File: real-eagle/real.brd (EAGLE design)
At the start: 104.1 x 123.4 mm, 49 parts, among them J2 POWER_JACK

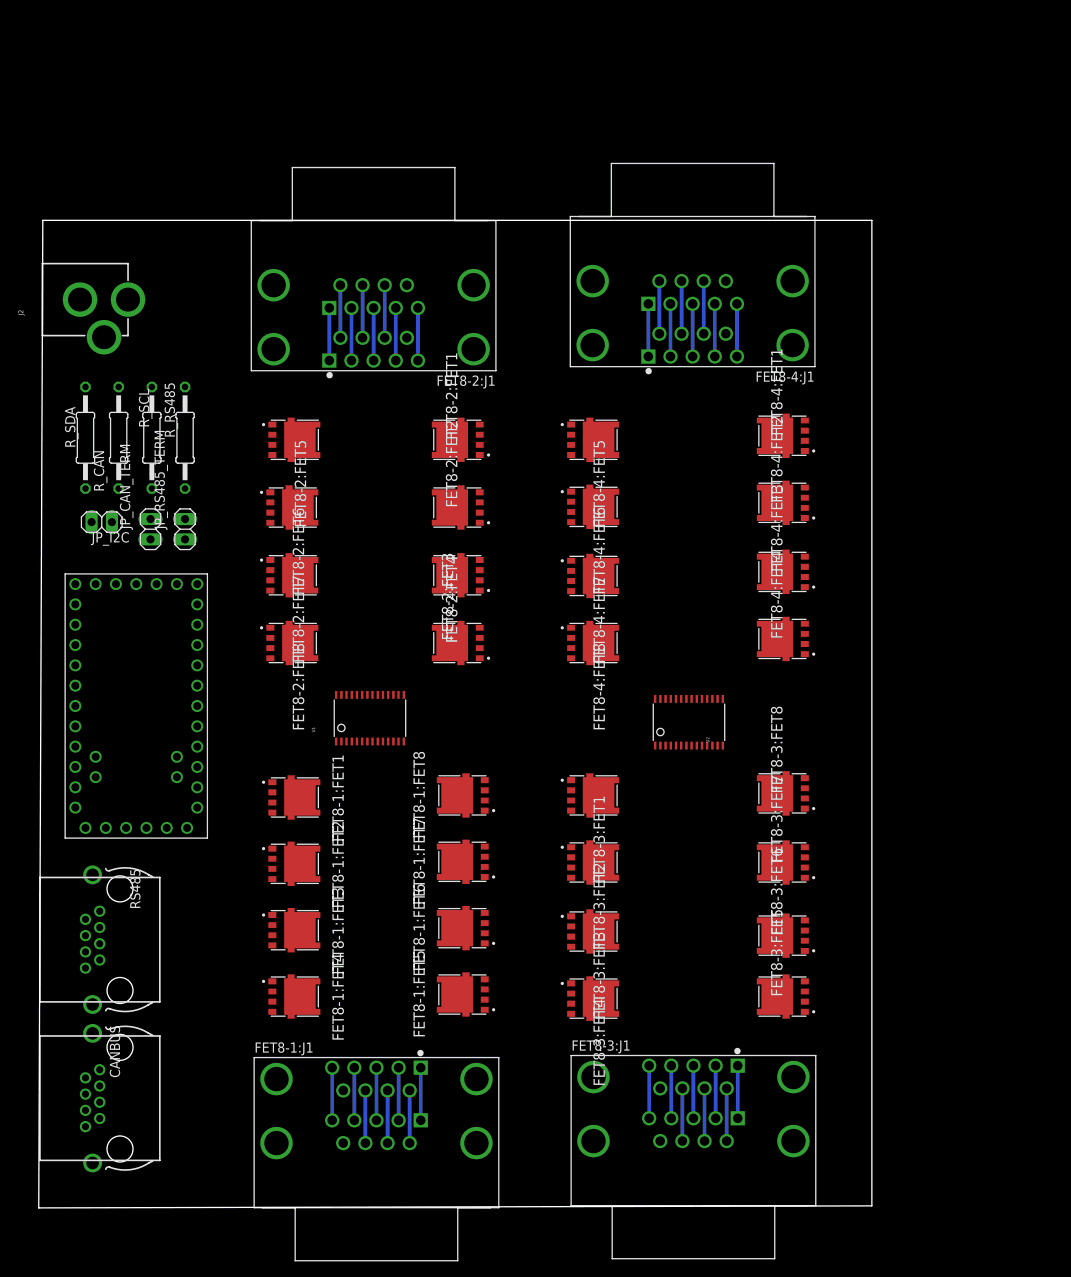
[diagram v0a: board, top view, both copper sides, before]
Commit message: Basis for routing
Route commands:

auto PWM_A0 PWM_A1 PWM_A2 PWM_A3 PWM_A4 PWM_A5 PWM_A6 PWM_A7 HEATER_A0 HEATER_A1 HEATER_A2 HEATER_A3 HEATER_A4 HEATER_A5 HEATER_A6 HEATER_A7 PWM_B0 PWM_B1 PWM_B2 PWM_B3 PWM_B4 PWM_B5 PWM_B6 PWM_B7 HEATER_B0 HEATER_B1 HEATER_B2 HEATER_B3 HEATER_B4 HEATER_B5 HEATER_B6 HEATER_B7

auto PWM_C0 PWM_C1 PWM_C2 PWM_C3 PWM_C4 PWM_C5 PWM_C6 PWM_C7 HEATER_C0 HEATER_C1 HEATER_C2 HEATER_C3 HEATER_C4 HEATER_C5 HEATER_C6 HEATER_C7 PWM_D0 PWM_D1 PWM_D2 PWM_D3 PWM_D4 PWM_D5 PWM_D6 PWM_D7 HEATER_D0 HEATER_D1 HEATER_D2 HEATER_D3 HEATER_D4 HEATER_D5 HEATER_D6 HEATER_D7

auto ! gnd
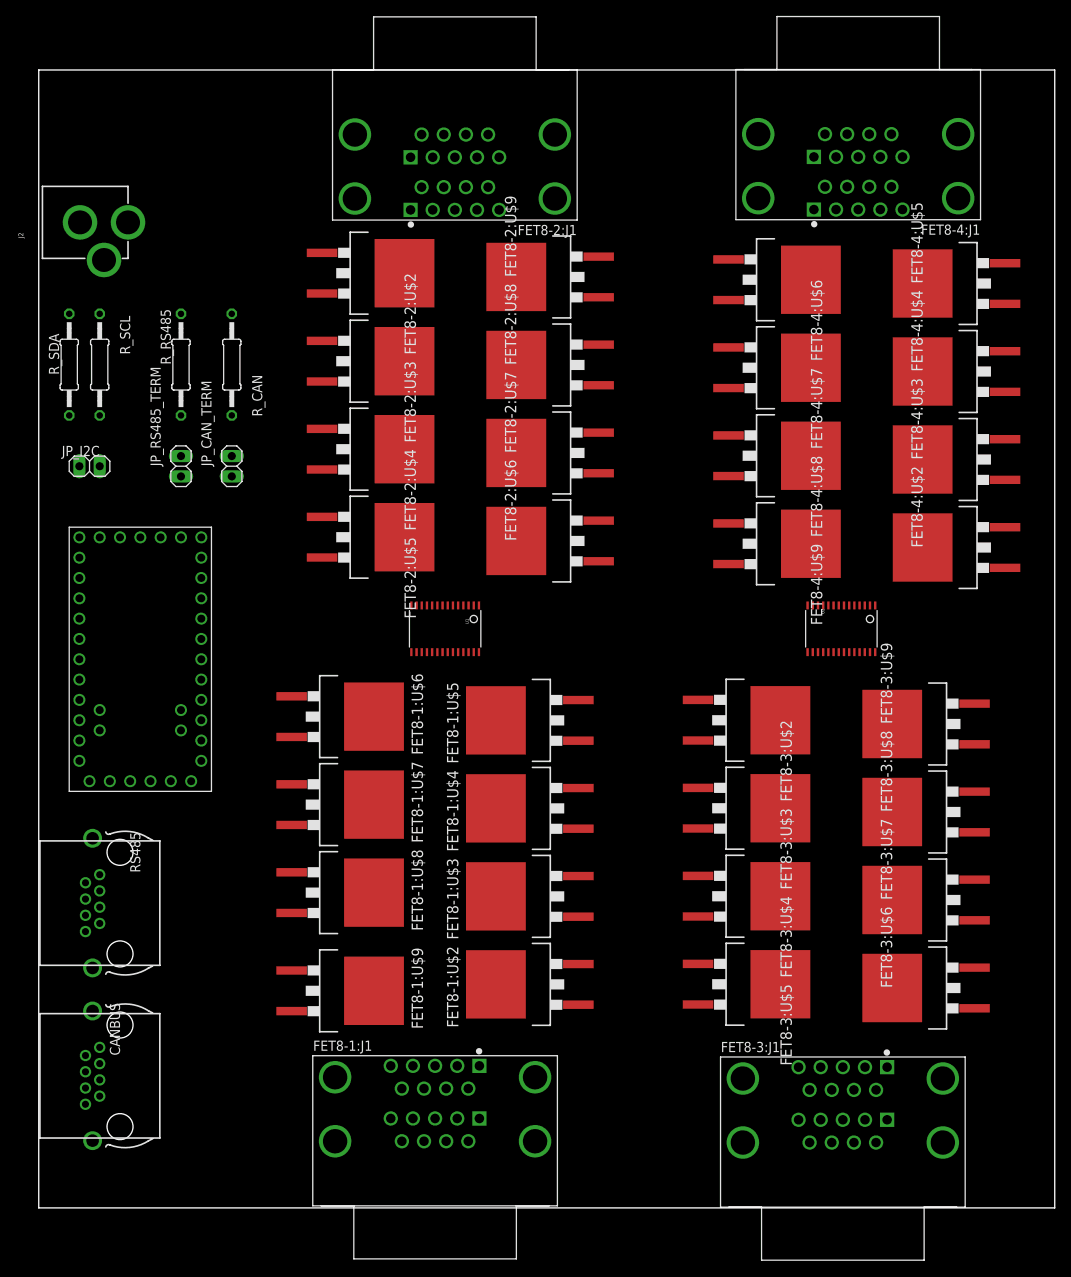
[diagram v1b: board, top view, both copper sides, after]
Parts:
- removed FET8-1:FET1, FET8-1:FET2, FET8-1:FET3, FET8-1:FET4, FET8-1:FET5, FET8-1:FET6, FET8-1:FET7, FET8-1:FET8, FET8-2:FET1, FET8-2:FET2, FET8-2:FET3, FET8-2:FET4, FET8-2:FET5, FET8-2:FET6, FET8-2:FET7, FET8-2:FET8, FET8-3:FET1, FET8-3:FET2, FET8-3:FET3, FET8-3:FET4, FET8-3:FET5, FET8-3:FET6, FET8-3:FET7, FET8-3:FET8, FET8-4:FET1, FET8-4:FET2, FET8-4:FET3, FET8-4:FET4, FET8-4:FET5, FET8-4:FET6, FET8-4:FET7, FET8-4:FET8: ONSEMI_FET_NVMFS5C604NL, real_library:DFN500X600X110-5N
- added FET8-1:U$2, FET8-1:U$3, FET8-1:U$4, FET8-1:U$5, FET8-1:U$6, FET8-1:U$7, FET8-1:U$8, FET8-1:U$9, FET8-2:U$2, FET8-2:U$3, FET8-2:U$4, FET8-2:U$5, FET8-2:U$6, FET8-2:U$7, FET8-2:U$8, FET8-2:U$9, FET8-3:U$2, FET8-3:U$3, FET8-3:U$4, FET8-3:U$5, FET8-3:U$6, FET8-3:U$7, FET8-3:U$8, FET8-3:U$9, FET8-4:U$2, FET8-4:U$3, FET8-4:U$4, FET8-4:U$5, FET8-4:U$6, FET8-4:U$7, FET8-4:U$8, FET8-4:U$9: NEXFET_CSD18542KTT, real_library:D2PAK-KTT
- moved FET8-4:J1 27.7 mm to (96.9, 91.8)
- moved U2 22.3 mm to (100.3, 39.4), turned to 180 degrees
- moved FET8-2:J1 21.4 mm to (46.5, 91.7)
- moved FET8-3:J1 18.7 mm to (106.1, -15.4)
- moved U1 14.6 mm to (50.8, 39.4), turned to 180 degrees
- moved R_CAN 13.5 mm to (24.1, 72.4)
- moved JP_CAN_TERM 12.9 mm to (24.1, 59.7)
- moved J2 9.65 mm to (-2.54, 90.2)
- moved R_SCL 9.45 mm to (7.62, 72.4)
- moved R_SDA 9.37 mm to (3.81, 72.4)
- moved R_RS485 9.16 mm to (17.8, 72.4)
- moved JP_RS485_TERM 7.89 mm to (17.8, 59.7)
- moved FET8-1:J1 7.33 mm to (55.1, -15.3)
- moved JP_I2C 7.15 mm to (6.35, 59.7), turned to 180 degrees
- moved U$1 5.86 mm to (12.7, 35.6)
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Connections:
- net GND: now also FET8-1:U$2.3, FET8-1:U$3.3, FET8-1:U$4.3, FET8-1:U$5.3, FET8-1:U$6.3, FET8-1:U$7.3, FET8-1:U$8.3, FET8-1:U$9.3, FET8-2:U$2.3, FET8-2:U$3.3, FET8-2:U$4.3, FET8-2:U$5.3, FET8-2:U$6.3, FET8-2:U$7.3, FET8-2:U$8.3, FET8-2:U$9.3, FET8-3:U$2.3, FET8-3:U$3.3, FET8-3:U$4.3, FET8-3:U$5.3, FET8-3:U$6.3, FET8-3:U$7.3, FET8-3:U$8.3, FET8-3:U$9.3, FET8-4:U$2.3, FET8-4:U$3.3, FET8-4:U$4.3, FET8-4:U$5.3, FET8-4:U$6.3, FET8-4:U$7.3, FET8-4:U$8.3, FET8-4:U$9.3; no longer FET8-1:FET1.1, FET8-1:FET1.2, FET8-1:FET1.3, FET8-1:FET2.1, FET8-1:FET2.2, FET8-1:FET2.3, FET8-1:FET3.1, FET8-1:FET3.2, FET8-1:FET3.3, FET8-1:FET4.1, FET8-1:FET4.2, FET8-1:FET4.3, FET8-1:FET5.1, FET8-1:FET5.2, FET8-1:FET5.3, FET8-1:FET6.1, FET8-1:FET6.2, FET8-1:FET6.3, FET8-1:FET7.1, FET8-1:FET7.2, FET8-1:FET7.3, FET8-1:FET8.1, FET8-1:FET8.2, FET8-1:FET8.3, FET8-2:FET1.1, FET8-2:FET1.2, FET8-2:FET1.3, FET8-2:FET2.1, FET8-2:FET2.2, FET8-2:FET2.3, FET8-2:FET3.1, FET8-2:FET3.2, FET8-2:FET3.3, FET8-2:FET4.1, FET8-2:FET4.2, FET8-2:FET4.3, FET8-2:FET5.1, FET8-2:FET5.2, FET8-2:FET5.3, FET8-2:FET6.1, FET8-2:FET6.2, FET8-2:FET6.3, FET8-2:FET7.1, FET8-2:FET7.2, FET8-2:FET7.3, FET8-2:FET8.1, FET8-2:FET8.2, FET8-2:FET8.3, FET8-3:FET1.1, FET8-3:FET1.2, FET8-3:FET1.3, FET8-3:FET2.1, FET8-3:FET2.2, FET8-3:FET2.3, FET8-3:FET3.1, FET8-3:FET3.2, FET8-3:FET3.3, FET8-3:FET4.1, FET8-3:FET4.2, FET8-3:FET4.3, FET8-3:FET5.1, FET8-3:FET5.2, FET8-3:FET5.3, FET8-3:FET6.1, FET8-3:FET6.2, FET8-3:FET6.3, FET8-3:FET7.1, FET8-3:FET7.2, FET8-3:FET7.3, FET8-3:FET8.1, FET8-3:FET8.2, FET8-3:FET8.3, FET8-4:FET1.1, FET8-4:FET1.2, FET8-4:FET1.3, FET8-4:FET2.1, FET8-4:FET2.2, FET8-4:FET2.3, FET8-4:FET3.1, FET8-4:FET3.2, FET8-4:FET3.3, FET8-4:FET4.1, FET8-4:FET4.2, FET8-4:FET4.3, FET8-4:FET5.1, FET8-4:FET5.2, FET8-4:FET5.3, FET8-4:FET6.1, FET8-4:FET6.2, FET8-4:FET6.3, FET8-4:FET7.1, FET8-4:FET7.2, FET8-4:FET7.3, FET8-4:FET8.1, FET8-4:FET8.2, FET8-4:FET8.3
- net HEATER_A0: now also FET8-1:U$2.2; no longer FET8-1:FET1.5@1, FET8-1:FET1.5@2, FET8-1:FET1.5@3, FET8-1:FET1.5@4, FET8-1:FET1.5@5
- net HEATER_A1: now also FET8-1:U$3.2; no longer FET8-1:FET2.5@1, FET8-1:FET2.5@2, FET8-1:FET2.5@3, FET8-1:FET2.5@4, FET8-1:FET2.5@5
- net HEATER_A2: now also FET8-1:U$4.2; no longer FET8-1:FET3.5@1, FET8-1:FET3.5@2, FET8-1:FET3.5@3, FET8-1:FET3.5@4, FET8-1:FET3.5@5
- net HEATER_A3: now also FET8-1:U$5.2; no longer FET8-1:FET4.5@1, FET8-1:FET4.5@2, FET8-1:FET4.5@3, FET8-1:FET4.5@4, FET8-1:FET4.5@5
- net HEATER_A4: now also FET8-1:U$6.2; no longer FET8-1:FET5.5@1, FET8-1:FET5.5@2, FET8-1:FET5.5@3, FET8-1:FET5.5@4, FET8-1:FET5.5@5
- net HEATER_A5: now also FET8-1:U$7.2; no longer FET8-1:FET6.5@1, FET8-1:FET6.5@2, FET8-1:FET6.5@3, FET8-1:FET6.5@4, FET8-1:FET6.5@5
- net HEATER_A6: now also FET8-1:U$8.2; no longer FET8-1:FET7.5@1, FET8-1:FET7.5@2, FET8-1:FET7.5@3, FET8-1:FET7.5@4, FET8-1:FET7.5@5
- net HEATER_A7: now also FET8-1:U$9.2; no longer FET8-1:FET8.5@1, FET8-1:FET8.5@2, FET8-1:FET8.5@3, FET8-1:FET8.5@4, FET8-1:FET8.5@5
- net HEATER_B0: now also FET8-2:U$2.2; no longer FET8-2:FET1.5@1, FET8-2:FET1.5@2, FET8-2:FET1.5@3, FET8-2:FET1.5@4, FET8-2:FET1.5@5
- net HEATER_B1: now also FET8-2:U$3.2; no longer FET8-2:FET2.5@1, FET8-2:FET2.5@2, FET8-2:FET2.5@3, FET8-2:FET2.5@4, FET8-2:FET2.5@5
- net HEATER_B2: now also FET8-2:U$4.2; no longer FET8-2:FET3.5@1, FET8-2:FET3.5@2, FET8-2:FET3.5@3, FET8-2:FET3.5@4, FET8-2:FET3.5@5
- net HEATER_B3: now also FET8-2:U$5.2; no longer FET8-2:FET4.5@1, FET8-2:FET4.5@2, FET8-2:FET4.5@3, FET8-2:FET4.5@4, FET8-2:FET4.5@5
- net HEATER_B4: now also FET8-2:U$6.2; no longer FET8-2:FET5.5@1, FET8-2:FET5.5@2, FET8-2:FET5.5@3, FET8-2:FET5.5@4, FET8-2:FET5.5@5
- net HEATER_B5: now also FET8-2:U$7.2; no longer FET8-2:FET6.5@1, FET8-2:FET6.5@2, FET8-2:FET6.5@3, FET8-2:FET6.5@4, FET8-2:FET6.5@5
- net HEATER_B6: now also FET8-2:U$8.2; no longer FET8-2:FET7.5@1, FET8-2:FET7.5@2, FET8-2:FET7.5@3, FET8-2:FET7.5@4, FET8-2:FET7.5@5
- net HEATER_B7: now also FET8-2:U$9.2; no longer FET8-2:FET8.5@1, FET8-2:FET8.5@2, FET8-2:FET8.5@3, FET8-2:FET8.5@4, FET8-2:FET8.5@5
- net HEATER_C0: now also FET8-3:U$2.2; no longer FET8-3:FET1.5@1, FET8-3:FET1.5@2, FET8-3:FET1.5@3, FET8-3:FET1.5@4, FET8-3:FET1.5@5
- net HEATER_C1: now also FET8-3:U$3.2; no longer FET8-3:FET2.5@1, FET8-3:FET2.5@2, FET8-3:FET2.5@3, FET8-3:FET2.5@4, FET8-3:FET2.5@5
- net HEATER_C2: now also FET8-3:U$4.2; no longer FET8-3:FET3.5@1, FET8-3:FET3.5@2, FET8-3:FET3.5@3, FET8-3:FET3.5@4, FET8-3:FET3.5@5
- net HEATER_C3: now also FET8-3:U$5.2; no longer FET8-3:FET4.5@1, FET8-3:FET4.5@2, FET8-3:FET4.5@3, FET8-3:FET4.5@4, FET8-3:FET4.5@5
- net HEATER_C4: now also FET8-3:U$6.2; no longer FET8-3:FET5.5@1, FET8-3:FET5.5@2, FET8-3:FET5.5@3, FET8-3:FET5.5@4, FET8-3:FET5.5@5
- net HEATER_C5: now also FET8-3:U$7.2; no longer FET8-3:FET6.5@1, FET8-3:FET6.5@2, FET8-3:FET6.5@3, FET8-3:FET6.5@4, FET8-3:FET6.5@5
- net HEATER_C6: now also FET8-3:U$8.2; no longer FET8-3:FET7.5@1, FET8-3:FET7.5@2, FET8-3:FET7.5@3, FET8-3:FET7.5@4, FET8-3:FET7.5@5
- net HEATER_C7: now also FET8-3:U$9.2; no longer FET8-3:FET8.5@1, FET8-3:FET8.5@2, FET8-3:FET8.5@3, FET8-3:FET8.5@4, FET8-3:FET8.5@5
- net HEATER_D0: now also FET8-4:U$2.2; no longer FET8-4:FET1.5@1, FET8-4:FET1.5@2, FET8-4:FET1.5@3, FET8-4:FET1.5@4, FET8-4:FET1.5@5
- net HEATER_D1: now also FET8-4:U$3.2; no longer FET8-4:FET2.5@1, FET8-4:FET2.5@2, FET8-4:FET2.5@3, FET8-4:FET2.5@4, FET8-4:FET2.5@5
- net HEATER_D2: now also FET8-4:U$4.2; no longer FET8-4:FET3.5@1, FET8-4:FET3.5@2, FET8-4:FET3.5@3, FET8-4:FET3.5@4, FET8-4:FET3.5@5
- net HEATER_D3: now also FET8-4:U$5.2; no longer FET8-4:FET4.5@1, FET8-4:FET4.5@2, FET8-4:FET4.5@3, FET8-4:FET4.5@4, FET8-4:FET4.5@5
- net HEATER_D4: now also FET8-4:U$6.2; no longer FET8-4:FET5.5@1, FET8-4:FET5.5@2, FET8-4:FET5.5@3, FET8-4:FET5.5@4, FET8-4:FET5.5@5
- net HEATER_D5: now also FET8-4:U$7.2; no longer FET8-4:FET6.5@1, FET8-4:FET6.5@2, FET8-4:FET6.5@3, FET8-4:FET6.5@4, FET8-4:FET6.5@5
- net HEATER_D6: now also FET8-4:U$8.2; no longer FET8-4:FET7.5@1, FET8-4:FET7.5@2, FET8-4:FET7.5@3, FET8-4:FET7.5@4, FET8-4:FET7.5@5
- net HEATER_D7: now also FET8-4:U$9.2; no longer FET8-4:FET8.5@1, FET8-4:FET8.5@2, FET8-4:FET8.5@3, FET8-4:FET8.5@4, FET8-4:FET8.5@5
- net PWM_A0: now also FET8-1:U$2.1; no longer FET8-1:FET1.4
- net PWM_A1: now also FET8-1:U$3.1; no longer FET8-1:FET2.4
- net PWM_A2: now also FET8-1:U$4.1; no longer FET8-1:FET3.4
- net PWM_A3: now also FET8-1:U$5.1; no longer FET8-1:FET4.4
- net PWM_A4: now also FET8-1:U$6.1; no longer FET8-1:FET5.4
- net PWM_A5: now also FET8-1:U$7.1; no longer FET8-1:FET6.4
- net PWM_A6: now also FET8-1:U$8.1; no longer FET8-1:FET7.4
- net PWM_A7: now also FET8-1:U$9.1; no longer FET8-1:FET8.4
- net PWM_B0: now also FET8-2:U$2.1; no longer FET8-2:FET1.4
- net PWM_B1: now also FET8-2:U$3.1; no longer FET8-2:FET2.4
- net PWM_B2: now also FET8-2:U$4.1; no longer FET8-2:FET3.4
- net PWM_B3: now also FET8-2:U$5.1; no longer FET8-2:FET4.4
- net PWM_B4: now also FET8-2:U$6.1; no longer FET8-2:FET5.4
- net PWM_B5: now also FET8-2:U$7.1; no longer FET8-2:FET6.4
- net PWM_B6: now also FET8-2:U$8.1; no longer FET8-2:FET7.4
- net PWM_B7: now also FET8-2:U$9.1; no longer FET8-2:FET8.4
- net PWM_C0: now also FET8-3:U$2.1; no longer FET8-3:FET1.4
- net PWM_C1: now also FET8-3:U$3.1; no longer FET8-3:FET2.4
- net PWM_C2: now also FET8-3:U$4.1; no longer FET8-3:FET3.4
- net PWM_C3: now also FET8-3:U$5.1; no longer FET8-3:FET4.4
- net PWM_C4: now also FET8-3:U$6.1; no longer FET8-3:FET5.4
- net PWM_C5: now also FET8-3:U$7.1; no longer FET8-3:FET6.4
- net PWM_C6: now also FET8-3:U$8.1; no longer FET8-3:FET7.4
- net PWM_C7: now also FET8-3:U$9.1; no longer FET8-3:FET8.4
- net PWM_D0: now also FET8-4:U$2.1; no longer FET8-4:FET1.4
- net PWM_D1: now also FET8-4:U$3.1; no longer FET8-4:FET2.4
- net PWM_D2: now also FET8-4:U$4.1; no longer FET8-4:FET3.4
- net PWM_D3: now also FET8-4:U$5.1; no longer FET8-4:FET4.4
- net PWM_D4: now also FET8-4:U$6.1; no longer FET8-4:FET5.4
- net PWM_D5: now also FET8-4:U$7.1; no longer FET8-4:FET6.4
- net PWM_D6: now also FET8-4:U$8.1; no longer FET8-4:FET7.4
- net PWM_D7: now also FET8-4:U$9.1; no longer FET8-4:FET8.4
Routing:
- net HEATER_D2: track 6.58 -> 0.00 mm
- net HEATER_D1: track 6.58 -> 0.00 mm
- net HEATER_D0: track 6.58 -> 0.00 mm
- net HEATER_B7: track 6.58 -> 0.00 mm
- net HEATER_B6: track 6.58 -> 0.00 mm
- net HEATER_B5: track 6.58 -> 0.00 mm
- net HEATER_B4: track 6.58 -> 0.00 mm
- net HEATER_B3: track 6.58 -> 0.00 mm
- net HEATER_A7: track 6.58 -> 0.00 mm
- net HEATER_A6: track 6.58 -> 0.00 mm
- net HEATER_A5: track 6.58 -> 0.00 mm
- net HEATER_A4: track 6.58 -> 0.00 mm
- net HEATER_A3: track 6.58 -> 0.00 mm
- net HEATER_A2: track 6.58 -> 0.00 mm
- net HEATER_A1: track 6.58 -> 0.00 mm
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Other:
- board size 104.1 x 123.4 mm -> 127 x 142.2 mm
